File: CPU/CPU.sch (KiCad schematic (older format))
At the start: 15 parts, among them J101 Conn_02x10_Odd_Even, J102 Conn_01x07_Female, Q101 IRLML0040TR, Q102 IRLML0040TR, SW101 SW_SPDT

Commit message: V5 Sent to fab.
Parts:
- SW101: footprint Marco:SWITCH_PCM12SMTR_SPDT -> MarcoK:SWITCH_SS312SAH4_SPDT
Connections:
- net +5VP: now also SW101.3 (C); no longer SW101.1 (A)
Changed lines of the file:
@@
 F 0 "SW101" V 5196 4512 50  0000 R CNN
 F 1 "SW_SPDT" V 5105 4512 50  0000 R CNN
-F 2 "Marco:SWITCH_PCM12SMTR_SPDT" H 5150 4700 50  0001 C CNN
+F 2 "MarcoK:SWITCH_SS312SAH4_SPDT" H 5150 4700 50  0001 C CNN
 F 3 "~" H 5150 4700 50  0001 C CNN
 F 4 "C221841" H 5150 4700 50  0001 C CNN "LCSC Part Number"
@@
 L power:+5VP #PWR0108
 U 1 1 5EB8BD82
-P 5050 4300
-F 0 "#PWR0108" H 5050 4150 50  0001 C CNN
-F 1 "+5VP" H 5065 4473 50  0000 C CNN
-F 2 "" H 5050 4300 50  0001 C CNN
-F 3 "" H 5050 4300 50  0001 C CNN
-	1    5050 4300
+P 5250 4300
+F 0 "#PWR0108" H 5250 4150 50  0001 C CNN
+F 1 "+5VP" H 5265 4473 50  0000 C CNN
+F 2 "" H 5250 4300 50  0001 C CNN
+F 3 "" H 5250 4300 50  0001 C CNN
+	1    5250 4300
 	1    0    0    -1
 $EndComp
@@
 L CPU-eagle-import:5V #SUPPLY?
 U 1 1 5EE216E8
-P 5250 4300
+P 5050 4300
 AR Path="/5E916134/5EE216E8" Ref="#SUPPLY?"  Part="1"
 AR Path="/5EE216E8" Ref="#SUPPLY0102"  Part="1"
-F 0 "#SUPPLY0102" H 5250 4300 50  0001 C CNN
-F 1 "5V" H 5250 4410 59  0000 C BNN
-F 2 "" H 5250 4300 50  0001 C CNN
-F 3 "" H 5250 4300 50  0001 C CNN
-	1    5250 4300
-	1    0    0    -1
-$EndComp
+F 0 "#SUPPLY0102" H 5050 4300 50  0001 C CNN
+F 1 "5V" H 5050 4410 59  0000 C BNN
+F 2 "" H 5050 4300 50  0001 C CNN
+F 3 "" H 5050 4300 50  0001 C CNN
+	1    5050 4300
+	1    0    0    -1
+$EndComp

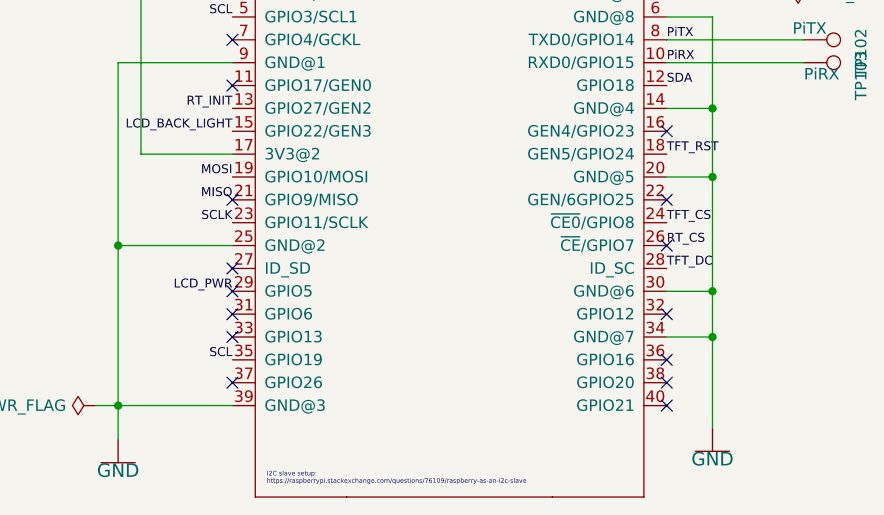
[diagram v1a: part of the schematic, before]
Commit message: Moved LED up a bit. Increased buffer space around mounting hole to keep vias away from screw head. It's alive! With RPi and LCD on board. Still need to get scroll wheel to connect.
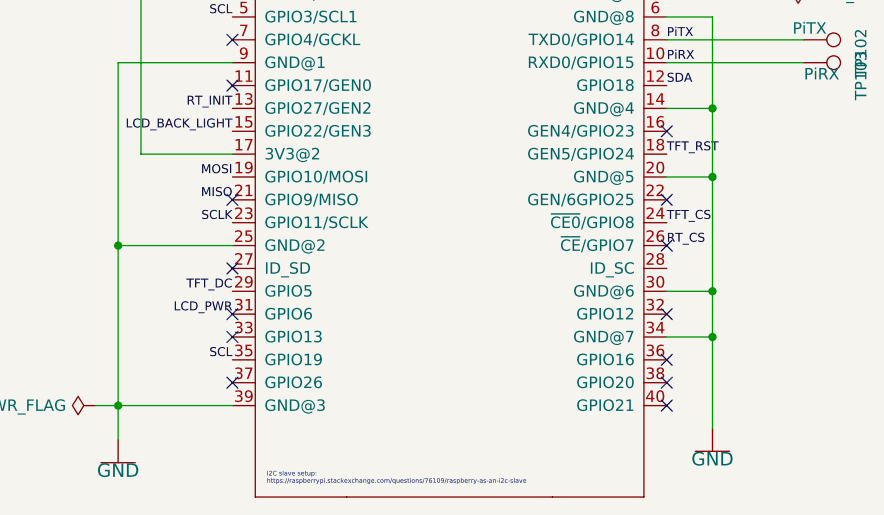
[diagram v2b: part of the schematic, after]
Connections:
- net LCD_PWR: now also Pi101.31 (GPIO6); no longer Pi101.29 (GPIO5)
- net TFT_DC: now also Pi101.29 (GPIO5); no longer Pi101.28 (ID_SC)
- no-connect marks 18 -> 17
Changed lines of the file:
@@
 Wire Wire Line
 	3300 2500 3300 2700
-Text Label 3050 6400 2    39   ~ 0
+Text Label 3050 6500 2    39   ~ 0
 LCD_PWR
 Wire Wire Line
@@
 Wire Wire Line
 	2650 5000 2650 4950
-NoConn ~ 3050 6400
 NoConn ~ 3050 6300
 Text Label 4950 6100 0    39   ~ 0
 TFT_CS
-Text Label 4950 6300 0    39   ~ 0
+Text Label 3050 6400 2    39   ~ 0
 TFT_DC
 $EndSCHEMATC
